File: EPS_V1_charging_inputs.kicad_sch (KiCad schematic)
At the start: 27 parts, among them U4 MP28167GQ-Z, U7 TPS2121RUXR

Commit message: Add other battery packs, connect all ALRT signals, assign footprints for new components, make inhibit switch footprints
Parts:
- C15: footprint (none) -> Capacitor_SMD:C_0603_1608Metric
- D5: footprint (none) -> LED_SMD:LED_0805_2012Metric
- R12, R13, R14, R15, R6, R7, R8, R9: footprint (none) -> Resistor_SMD:R_0603_1608Metric
- U7: footprint RUX0012A -> TPS2121RUXR:RUX0012A
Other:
- note added: "Selects between 5V external input and solar input, prefers external input if present"
- note removed: "Selects between 5V USBC input and solar input, prefers USBC input if present"
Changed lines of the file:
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@@
 		)
 	)
-	(text "Selects between 5V USBC input and solar input, prefers USBC input if present"
+	(text "Selects between 5V external input and solar input, prefers external input if present"
 		(exclude_from_sim no)
 		(at 195.58 23.622 0)
@@
 	)
 	(junction
+		(at 173.99 34.29)
+		(diameter 0)
+		(color 0 0 0 0)
+	)
+	(junction
 		(at 119.38 158.75)
 		(diameter 0)
@@
 	(wire
 		(pts
+			(xy 173.99 34.29) (xy 176.53 34.29)
+		)
+		(stroke
+			(width 0)
+			(type default)
+		)
+	)
+	(wire
+		(pts
 			(xy 176.53 138.43) (xy 181.61 138.43)
 		)
@@
 	(wire
 		(pts
-			(xy 153.67 34.29) (xy 176.53 34.29)
+			(xy 153.67 34.29) (xy 173.99 34.29)
 		)
 		(stroke
@@
 			)
 		)
-		(property "Footprint" ""
+		(property "Footprint" "Resistor_SMD:R_0603_1608Metric"
 			(at 104.394 74.676 90)
 			(hide yes)
@@
 			)
 		)
-		(property "Footprint" ""
+		(property "Footprint" "Resistor_SMD:R_0603_1608Metric"
 			(at 87.884 44.196 90)
 			(hide yes)
@@
 			)
 		)
-		(property "Footprint" ""
+		(property "Footprint" "LED_SMD:LED_0805_2012Metric"
 			(at 171.45 45.72 0)
 			(hide yes)
@@
 			)
 		)
-		(property "Footprint" ""
+		(property "Footprint" "Resistor_SMD:R_0603_1608Metric"
 			(at 76.454 55.626 90)
 			(hide yes)
@@
 			)
 		)
-		(property "Footprint" ""
+		(property "Footprint" "Resistor_SMD:R_0603_1608Metric"
 			(at 166.624 54.356 90)
 			(hide yes)
@@
 			)
 		)
-		(property "Footprint" ""
+		(property "Footprint" "Resistor_SMD:R_0603_1608Metric"
 			(at 159.766 46.736 90)
 			(hide yes)
@@
 			)
 		)
-		(property "Footprint" ""
+		(property "Footprint" "Capacitor_SMD:C_0603_1608Metric"
 			(at 160.9852 60.96 0)
 			(hide yes)
@@
 			)
 		)
-		(property "Footprint" ""
+		(property "Footprint" "Resistor_SMD:R_0603_1608Metric"
 			(at 87.884 55.626 90)
 			(hide yes)
@@
 			)
 		)
-		(property "Footprint" "RUX0012A"
+		(property "Footprint" "TPS2121RUXR:RUX0012A"
 			(at 133.35 49.53 0)
 			(hide yes)
@@
 			)
 		)
-		(property "Footprint" ""
+		(property "Footprint" "Resistor_SMD:R_0603_1608Metric"
 			(at 76.454 45.466 90)
 			(hide yes)
@@
 			)
 		)
-		(property "Footprint" ""
+		(property "Footprint" "Resistor_SMD:R_0603_1608Metric"
 			(at 104.394 63.246 90)
 			(hide yes)
@@
 					(unit 1)
 				)
+			)
+		)
+	)
+	(symbol
+		(lib_id "power:PWR_FLAG")
+		(at 173.99 34.29 0)
+		(unit 1)
+		(body_style 1)
+		(exclude_from_sim no)
+		(in_bom yes)
+		(on_board yes)
+		(in_pos_files yes)
+		(dnp no)
+		(fields_autoplaced yes)
+		(property "Reference" "#FLG03"
+			(at 173.99 32.385 0)
+			(hide yes)
+			(show_name no)
+			(do_not_autoplace no)
+			(effects
+				(font
+					(size 1.27 1.27)
+				)
+			)
+		)
+		(property "Value" "PWR_FLAG"
+			(at 173.99 29.21 0)
+			(show_name no)
+			(do_not_autoplace no)
+			(effects
+				(font
+					(size 1.27 1.27)
+				)
+			)
+		)
+		(property "Footprint" ""
+			(at 173.99 34.29 0)
+			(hide yes)
+			(show_name no)
+			(do_not_autoplace no)
+			(effects
+				(font
+					(size 1.27 1.27)
+				)
+			)
+		)
+		(property "Datasheet" ""
+			(at 173.99 34.29 0)
+			(hide yes)
+			(show_name no)
+			(do_not_autoplace no)
+			(effects
+				(font
+					(size 1.27 1.27)
+				)
+			)
+		)
+		(property "Description" "Special symbol for telling ERC where power comes from"
+			(at 173.99 34.29 0)
+			(hide yes)
+			(show_name no)
+			(do_not_autoplace no)
+			(effects
+				(font
+					(size 1.27 1.27)
+				)
+			)
+		)
+		(pin "1"
+		)
+		(instances
+			(project "EPS_V1"
+				(path "/85157432-5d03-48fa-ab40-27ed3d133f47/200409e9-92e5-48dc-b89e-cefaee3c74ba"
+					(reference "#FLG03")
+					(unit 1)
+				)

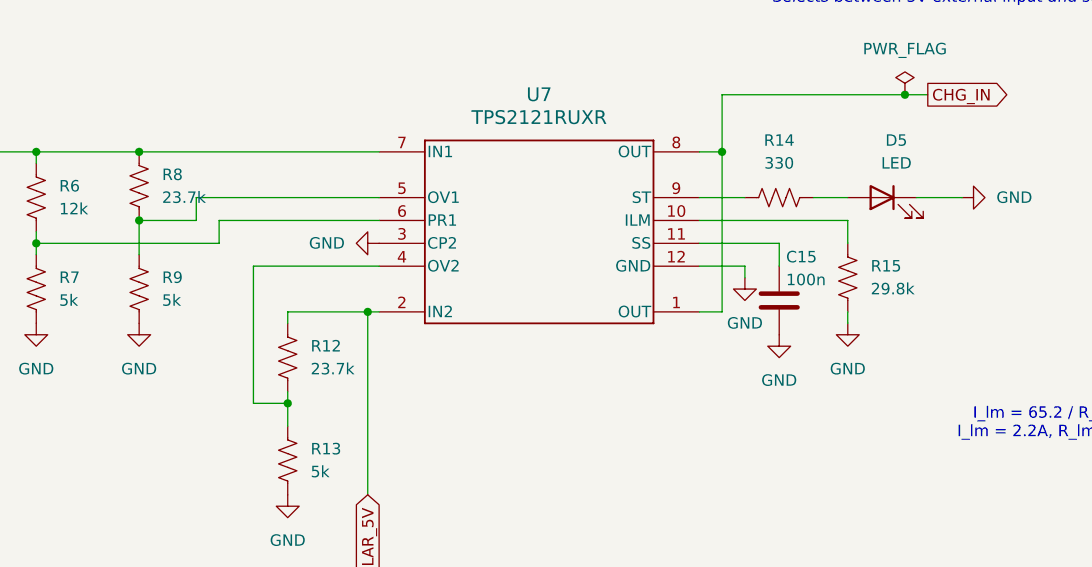
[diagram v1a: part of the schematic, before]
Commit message: Change new resistors to standard values
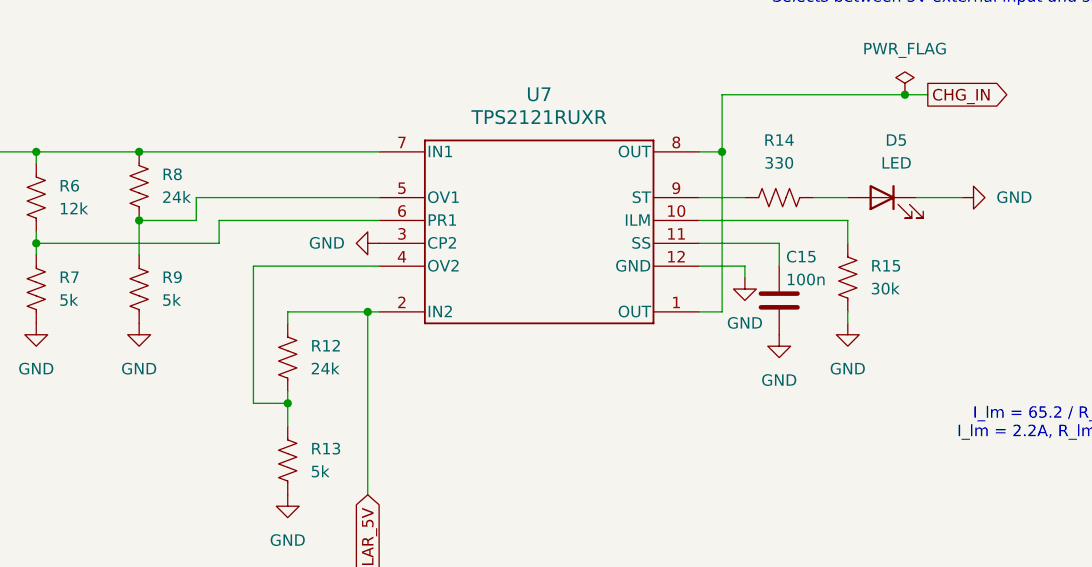
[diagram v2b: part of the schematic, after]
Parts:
- R12, R8: value 23.7k -> 24k
- R15: value 29.8k -> 30k
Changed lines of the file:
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@@
 			)
 		)
-		(property "Value" "23.7k"
+		(property "Value" "24k"
 			(at 91.44 45.7199 0)
 			(show_name no)
@@
 			)
 		)
-		(property "Value" "29.8k"
+		(property "Value" "30k"
 			(at 170.18 55.8799 0)
 			(show_name no)
@@
 			)
 		)
-		(property "Value" "23.7k"
+		(property "Value" "24k"
 			(at 107.95 64.7699 0)
 			(show_name no)
